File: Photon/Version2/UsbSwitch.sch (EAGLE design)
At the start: 23 parts, among them IC1 PHOTON, IC2 LM3526M-L, X1 USB A Socket, X2 USB A Socket

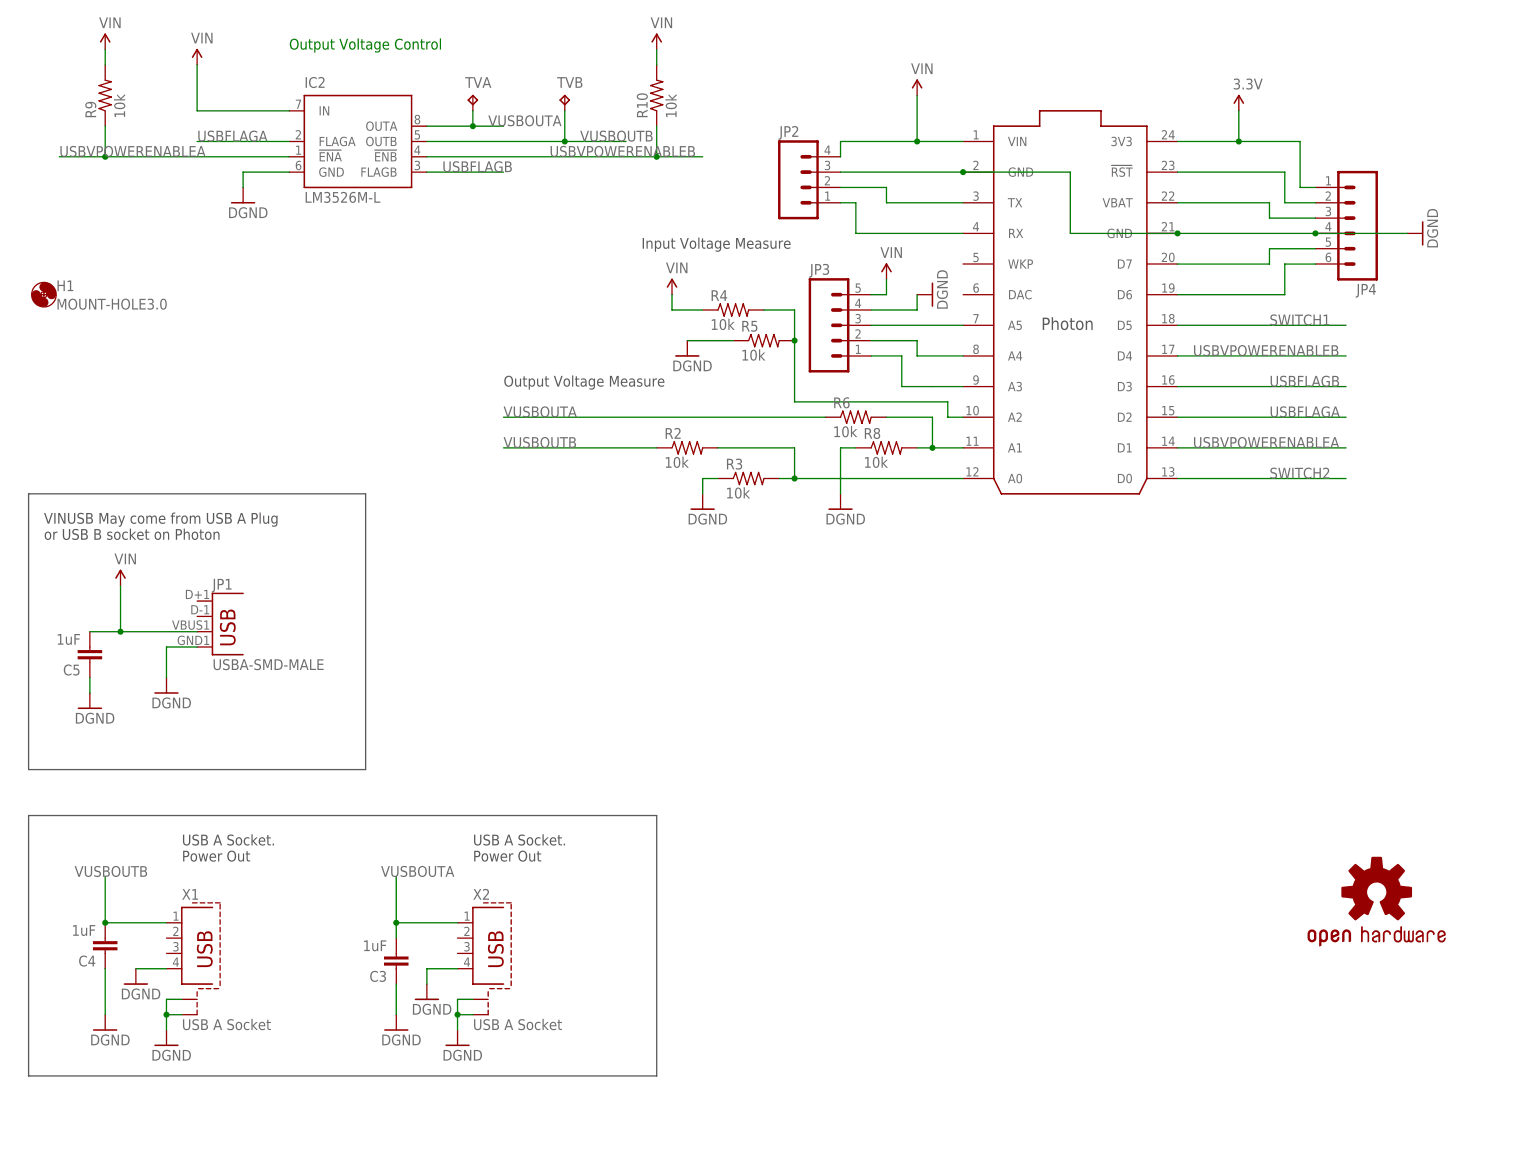
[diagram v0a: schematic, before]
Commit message: Moved USB connector to top bottom side of PCB so that the Photon sticks out from the wall when put in a wall plug and that the USB in/out is not flipped.
Moved USB controller chip inside the photon and put connectors for the photon pins all along appropriate pins.
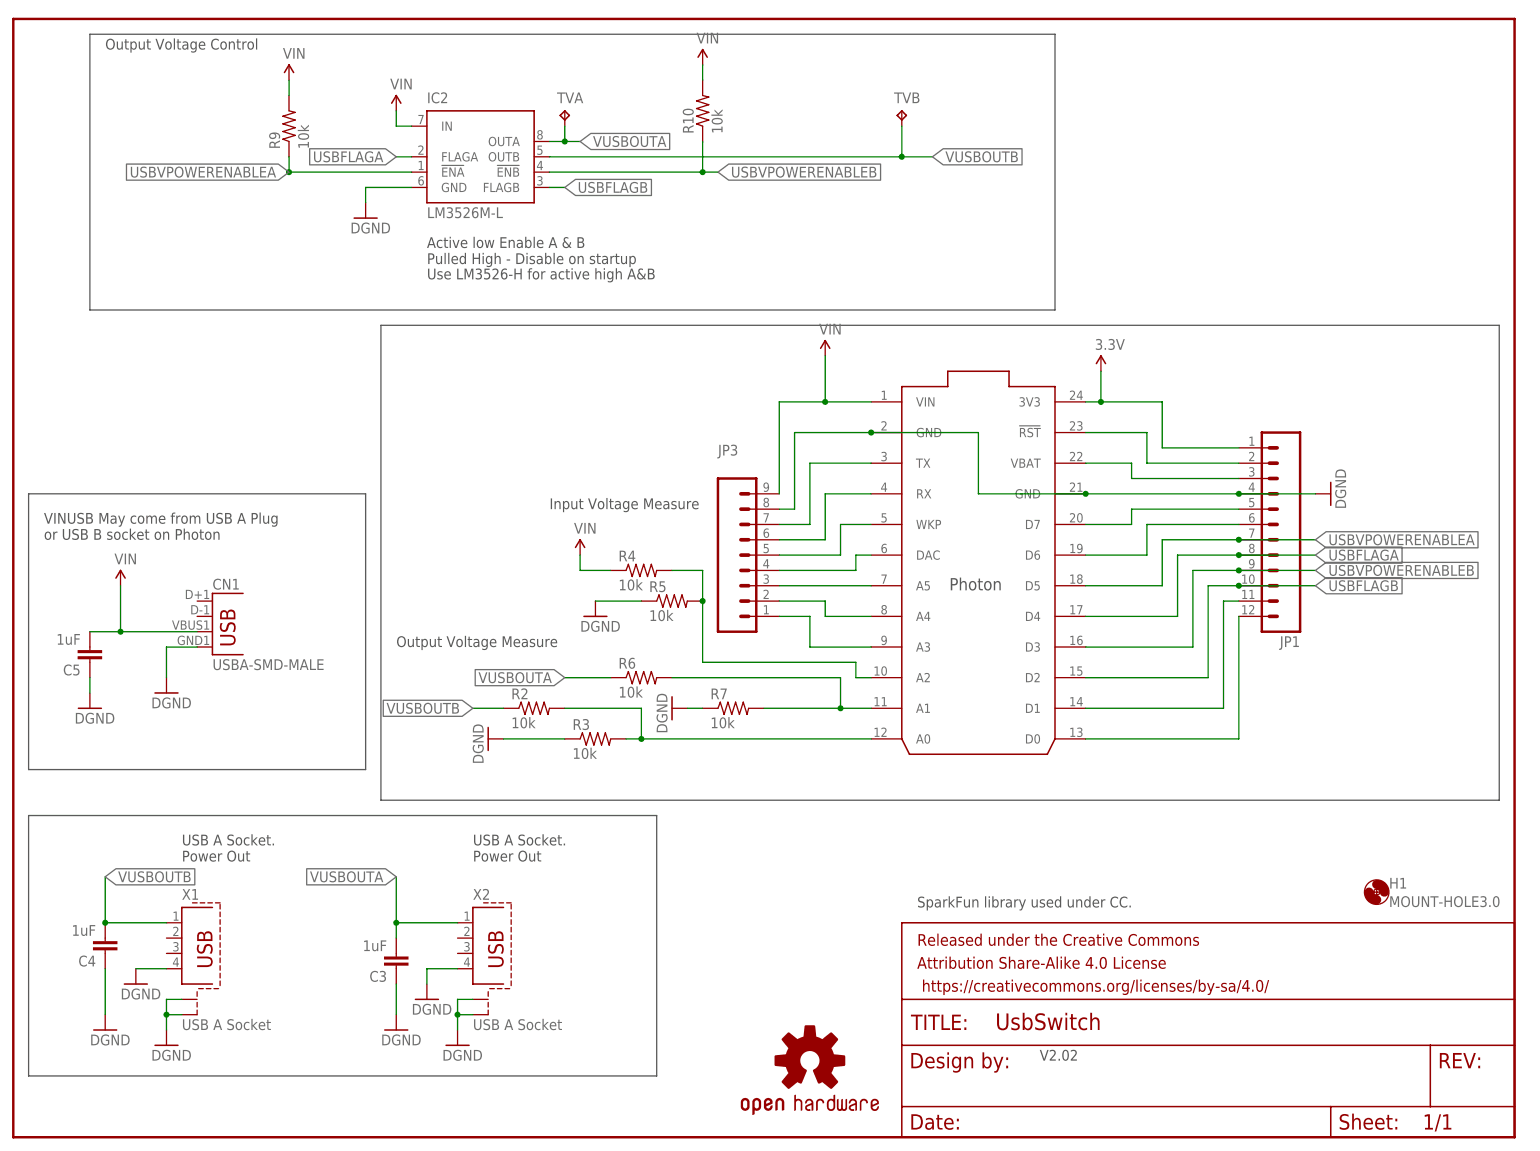
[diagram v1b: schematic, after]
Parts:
- removed JP2: (no value), SparkFun-Connectors:M04PTH
- removed JP4: (no value), SparkFun-Connectors:M06SILK_FEMALE_PTH
- removed R8: 10k, SparkFun-Passives:RESISTOR1206
- added CN1: USBA-SMD-MALE, SparkFun-Connectors:USBA-SMD-MALE
- added FRAME2: FRAME-LETTER, SparkFun-Aesthetics:FRAME-LETTER
- added R7: 10k, SparkFun-Passives:RESISTOR1206
- JP1: value USBA-SMD-MALE -> (none); device SparkFun-Connectors:USBA-SMD-MALE -> SparkFun-Connectors:M12PTH
- JP3: device SparkFun-Connectors:M05PTH -> SparkFun-Connectors:M09
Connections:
- removed net SWITCH1: IC1.D5
- removed net SWITCH2: IC1.D0
- new net N$1: IC1.DAC, JP3.4
- new net N$16: IC1.TX, JP3.7
- new net SCL/SWITCH2: IC1.D1, JP1.11
- new net SDA/SWITCH1: IC1.D0, JP1.12
- net 3.3V: now also JP1.1; no longer JP4.1
- net GND: now also CN1.GND, JP1.4, JP3.8, R7.1; no longer JP1.GND, JP2.3, JP3.4, JP4.4, R8.1
- net N$12: now also JP1.6; no longer JP4.6
- net N$13: now also JP1.5; no longer JP4.5
- net N$14: now also JP1.3; no longer JP4.3
- net N$15: now also JP1.2; no longer JP4.2
- net N$3: now also IC1.WKP, JP3.5; no longer IC1.TX, JP2.2
- net N$4: now also JP3.6; no longer JP2.1
- net N$5: now also R7.2; no longer R8.2
- net USBFLAGA: now also IC1.D4, JP1.8; no longer IC1.D2
- net USBFLAGB: now also IC1.D2, JP1.10; no longer IC1.D3
- net USBVPOWERENABLEA: now also IC1.D5, JP1.7; no longer IC1.D1
- net USBVPOWERENABLEB: now also IC1.D3, JP1.9; no longer IC1.D4
- net VIN: now also CN1.VBUS, JP3.9; no longer JP1.VBUS, JP2.4, JP3.5
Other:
- note added: "Active low Enable A & B Pulled High - Disable on startup"
- note added: "SparkFun library used under CC."
- note added: "Use LM3526-H for active high A&B"
- note added: "V2.02"
- moved on the sheet: H1, IC2, R10, R2, R3, R4, R5, R6, R9, TVA, TVB
